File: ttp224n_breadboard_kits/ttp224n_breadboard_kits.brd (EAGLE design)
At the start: 160 x 100 mm, 20 parts, among them U1 TTP224N-BSB

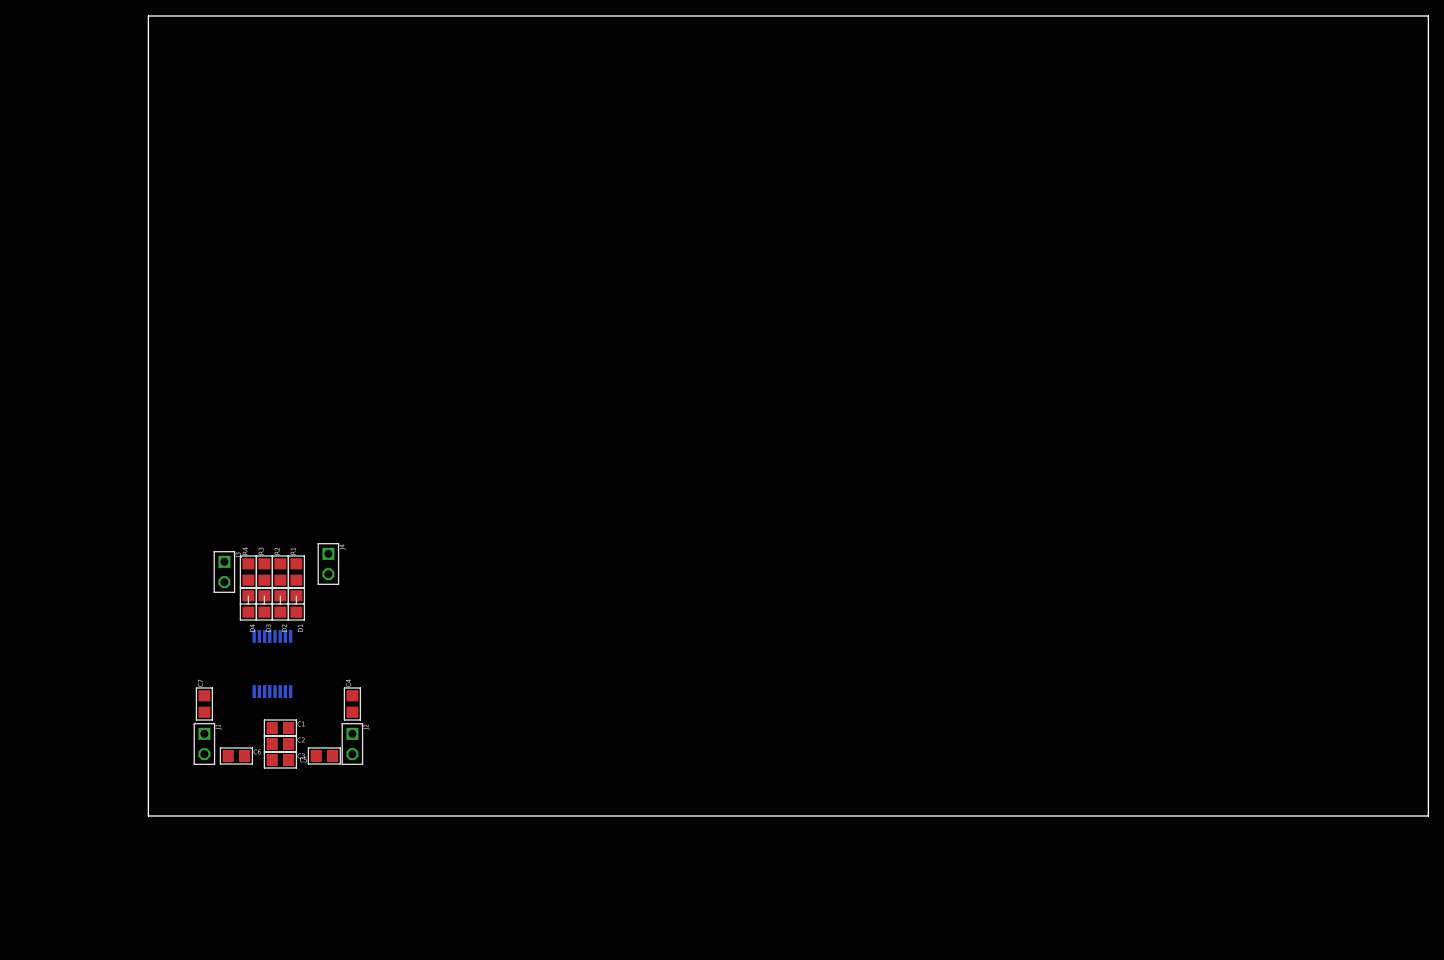
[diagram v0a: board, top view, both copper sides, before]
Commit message: the ttp224n breadboard kits is done
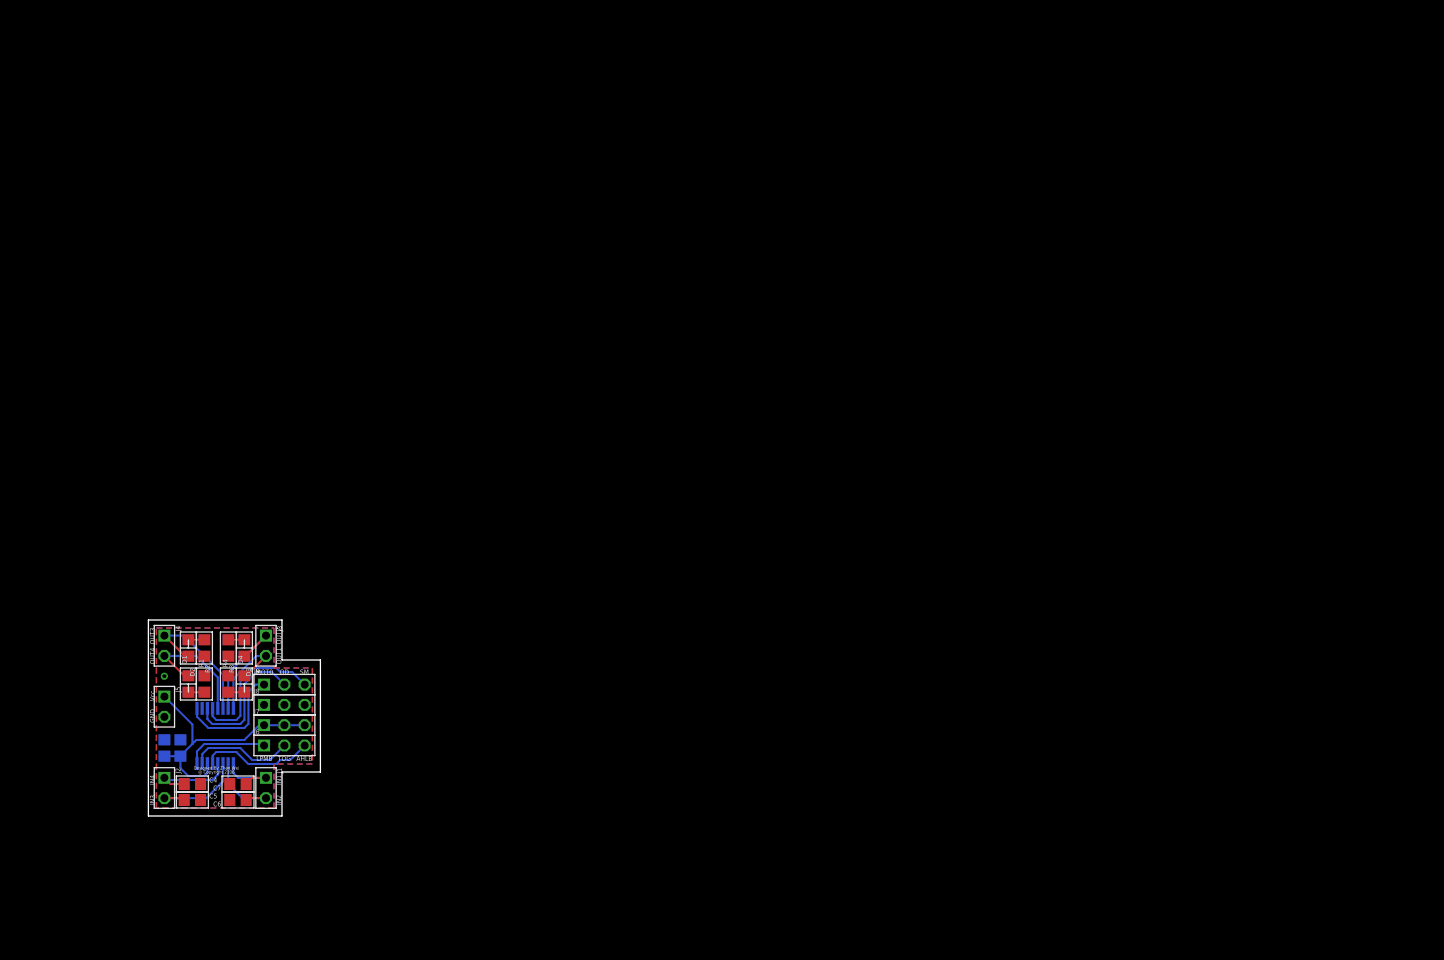
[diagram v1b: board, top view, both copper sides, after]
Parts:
- removed C1: 0.1uF, Capacitors:0805
- added J5: (no value), Connectors:2PIN_HEADER_PITCH2.54MM_TH
- added J6, J7, J8, J9: (no value), Connectors:3PIN_HEADER_PITCH2.54MM_TH
- C4, C5, C6, C7: value (none) -> 4.7uF
- moved J2 24.1 mm to (2.00, 3.50)
- moved J4 22.9 mm to (2.00, 21.3)
- moved C4 22.4 mm to (5.50, 4.00), turned to 0 degrees
- moved R1 18.1 mm to (7.00, 16.5)
- moved C5 17.4 mm to (5.50, 2.00), turned to 0 degrees
- moved D1 16.8 mm to (5.00, 16.5), turned to 90 degrees
- moved C3 14.6 mm to (2.00, 8.50), flipped to the bottom, turned to 90 degrees
- moved R4 14.2 mm to (10.0, 16.5)
- moved R2 13.4 mm to (7.00, 21.0), turned to 270 degrees
- moved D2 12.7 mm to (5.00, 21.0)
- moved C2 12.5 mm to (4.00, 8.50), flipped to the bottom, turned to 90 degrees
- moved U1 11.5 mm to (8.35, 10.0)
- moved C7 10.8 mm to (11.2, 4.00), turned to 180 degrees
- moved J3 10.6 mm to (14.7, 21.3)
- moved R3 10.5 mm to (10.0, 21.0), turned to 270 degrees
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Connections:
- net +3V3: now also J5.1, J7.1, J7.2, J7.3; no longer C1.1
- net AHLB: now also J6.3
- net DGND: now also J5.2, J8.1, J8.2, J8.3; no longer C1.2
- net LPMB: now also J6.1
- net MOT0: now also J9.1
- net OD: now also J9.2
- net SM: now also J9.3
- net TOG: now also J6.2
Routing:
- net +3V3: track 0.00 -> 33.1 mm
- net SM: track 0.00 -> 18.9 mm
- net OUT3: track 0.00 -> 17.6 mm
- net OD: track 0.00 -> 17.2 mm
- net OUT4: track 0.00 -> 15.8 mm
- net OUT2: track 0.00 -> 14.9 mm
- net MOT0: track 0.00 -> 14.6 mm
- net AHLB: track 0.00 -> 14.3 mm
- net TOG: track 0.00 -> 13.1 mm
- net IN3: track 0.00 -> 13.0 mm
- net OUT1: track 0.00 -> 12.7 mm
- net IN4: track 0.00 -> 11.2 mm
- net IN2: track 0.00 -> 10.6 mm
- net LPMB: track 0.00 -> 10.4 mm
- net IN1: track 0.00 -> 8.29 mm
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- added copper zone on layer 1, net DGND
- added copper zone on layer 16, net DGND
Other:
- board size 160 x 100 mm -> 21.5 x 24.5 mm
- board text added: "@ Copyright 2106"
- board text added: "AHLB"
- board text added: "Designed By Zhen Wei"
- board text added: "GND"
- board text added: "IN1"
- board text added: "IN2"
- board text added: "IN3"
- board text added: "IN4"
- board text added: "LPMB"
- board text added: "MOT0"
- board text added: "OD"
- board text added: "OUT1"
- board text added: "OUT2"
- board text added: "OUT3"
- board text added: "OUT4"
- board text added: "SM"
- board text added: "TOG"
- board text added: "Vcc"

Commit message: make the change and ttp224n_breadboard_kits is ready to go
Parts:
- moved J9 8.46 mm to (22.3, 9.85), turned to 270 degrees
- moved R3 6.53 mm to (9.35, 14.5)
- moved R2 6.51 mm to (7.35, 14.5)
- moved J8 4.90 mm to (19.8, 9.85), turned to 270 degrees
- moved C5 3.96 mm to (7.35, 5.50), turned to 90 degrees
- moved C6 3.96 mm to (9.35, 5.50), turned to 90 degrees
- moved D3 3.64 mm to (9.35, 18.5), turned to 90 degrees
- moved D2 3.43 mm to (7.35, 18.5), turned to 90 degrees
- moved R1 2.59 mm to (5.35, 14.5), turned to 270 degrees
- moved J3 2.54 mm to (14.7, 18.7), flipped to the bottom
- moved J4 2.54 mm to (2.00, 18.7), flipped to the bottom
- moved J6 2.52 mm to (14.7, 9.85), turned to 270 degrees
- moved R4 2.41 mm to (11.3, 14.5), turned to 270 degrees
- moved D4 2.10 mm to (11.3, 18.5)
- moved D1 2.03 mm to (5.35, 18.5)
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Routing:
- net IN1: track 8.29 -> 18.5 mm
- net IN4: track 11.2 -> 21.1 mm
- net IN2: track 10.6 -> 19.7 mm
- net SM: track 18.9 -> 27.4 mm
- net IN3: track 13.0 -> 20.8 mm
- net OD: track 17.2 -> 24.7 mm
- net MOT0: track 14.6 -> 20.9 mm
- net AHLB: track 14.3 -> 8.13 mm
- net +3V3: track 33.1 -> 38.1 mm
- net TOG: track 13.1 -> 10.0 mm
- net OUT4: track 15.8 -> 13.3 mm
- net OUT1: track 12.7 -> 10.6 mm
- net LPMB: track 10.4 -> 12.3 mm
- added copper zone on layer 1, net IN1
- added copper zone on layer 1, net IN2
- added copper zone on layer 1, net IN3
- added copper zone on layer 1, net IN4
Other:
- board size 21.5 x 24.5 mm -> 50 x 34.5 mm
- board text added: "1"
- board text added: "2"
- board text added: "3"
- board text added: "4"
- board text added: "@ Copyright 2107"
- board text removed: "@ Copyright 2106"

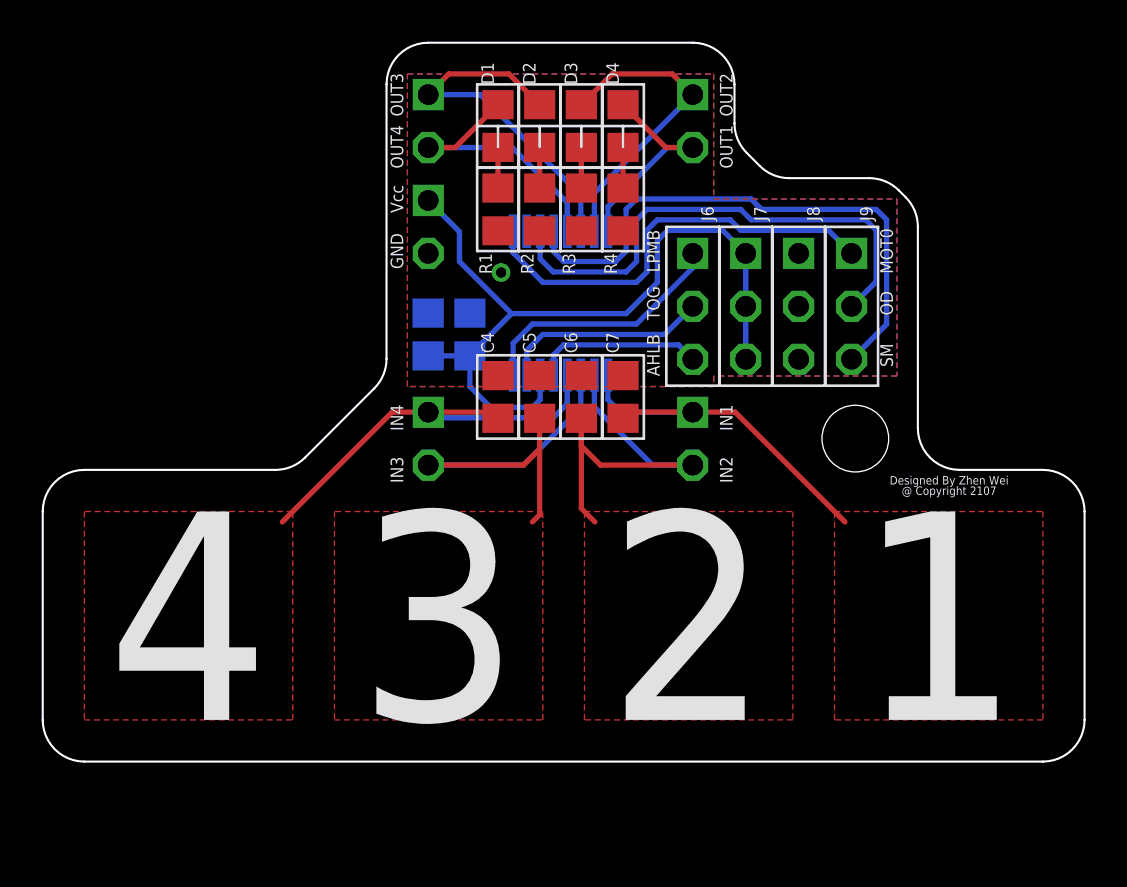
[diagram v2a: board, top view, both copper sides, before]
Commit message: update the ttp224 touchpad module
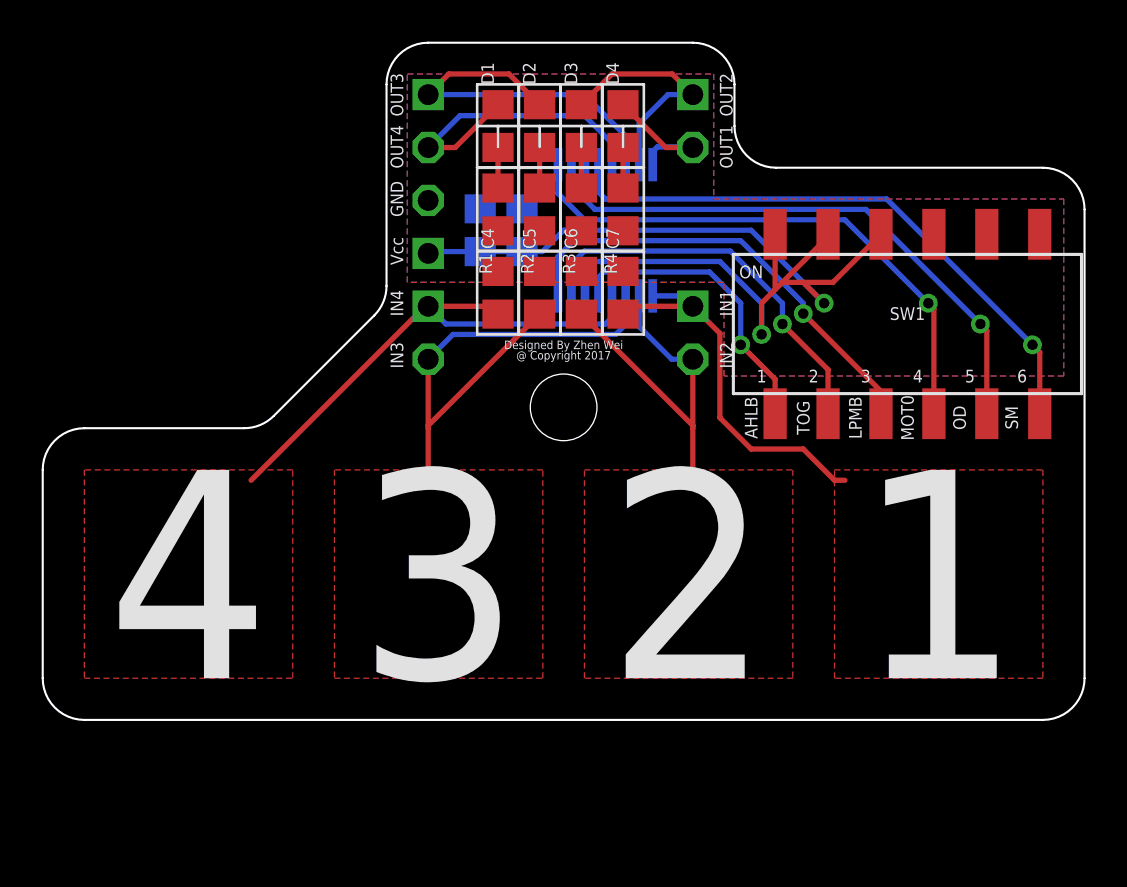
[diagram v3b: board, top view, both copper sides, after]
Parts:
- removed J6, J7, J8, J9: (no value), Connectors:3PIN_HEADER_PITCH2.54MM_TH
- added SW1: (no value), Switches:DIP_SW_219-6MST
- moved C3 6.73 mm to (6.50, 13.5)
- moved J1 5.08 mm to (14.7, 8.58)
- moved J2 5.08 mm to (2.00, 8.58)
- moved C2 5.02 mm to (4.50, 13.5)
- moved C4 5.00 mm to (5.35, 10.5)
- moved C5 5.00 mm to (7.35, 10.5)
- moved C6 5.00 mm to (9.35, 10.5)
- moved C7 5.00 mm to (11.3, 10.5)
- moved U1 4.11 mm to (10.5, 13.5)
- turned J5 to 90 degrees
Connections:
- net +3V3: now also SW1.2, SW1.4, SW1.6; no longer J7.1, J7.2, J7.3
- net AHLB: now also SW1.1; no longer J6.3
- net DGND: now also SW1.10, SW1.12, SW1.8; no longer J8.1, J8.2, J8.3
- net LPMB: now also SW1.5; no longer J6.1
- net MOT0: now also SW1.7; no longer J9.1
- net OD: now also SW1.9; no longer J9.2
- net SM: now also SW1.11; no longer J9.3
- net TOG: now also SW1.3; no longer J6.2
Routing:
- net +3V3: track 38.1 -> 49.0 mm, vias 0 -> 2
- net LPMB: track 12.3 -> 22.1 mm, vias 0 -> 1
- net TOG: track 10.0 -> 19.2 mm, vias 0 -> 1
- net AHLB: track 8.13 -> 14.4 mm, vias 0 -> 1
- net MOT0: track 20.9 -> 26.8 mm, vias 0 -> 1
- net IN4: track 21.1 -> 25.8 mm
- net IN3: track 20.8 -> 24.9 mm
- net OUT1: track 10.6 -> 6.86 mm
- net OUT2: track 14.9 -> 11.5 mm
- net OD: track 24.7 -> 27.6 mm, vias 0 -> 1
- net OUT4: track 13.3 -> 15.2 mm
- net IN2: track 19.7 -> 18.1 mm
- net SM: track 27.4 -> 28.6 mm, vias 0 -> 1
- net OUT3: track 17.4 -> 18.0 mm
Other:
- board size 50 x 34.5 mm -> 50 x 32.5 mm
- board text added: "@ Copyright 2017"
- board text removed: "@ Copyright 2107"
